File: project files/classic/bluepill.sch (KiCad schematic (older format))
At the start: 35 parts, among them J1 USB_B_Micro, J2 Boot, J3 Left Row, J4 Right Row, J5 SWD, SW1 Reset, U1 RT8183-33, U2 STM32F103C8Tx, Y1 8MHz, Y2 32768Hz

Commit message: re-arrangement + updated description
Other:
- note added: "BluePill boards from TaoBao have diferent design:\n+ extra 1M or 10M resistor between OSCIN | OSCOUT \n- no GND connection for capacitors\nSame concept can be found on some RedPill boards.\nRecommended design from STM has no resistor!\nIn this schematic it is OPTIONAL!\nBluePill uses crystal in HC-49S (HC-49-4H) package.\nBlackPill uses both: resistor (10M) and \ngrounding for capacitors.\nMapleM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"
- note added: "Typically used diodes:\n- 1N5819: in SOD123F or DO-41\n- LSM115JE3/TR13 : DO-214BA\n- BAS70 : in SOT23\n- 1N4448 : in SOD123\n- BAT54C : in SOT-23 : WeAct F4x1 DevBoards"
- note removed: "BluePill boards from TaoBao have diferent design:\n+ extra 1M or 10M resistor between OSCIN | OSCOUT \n- no GND connection for capacitors\nSame concept can be found on some RedPill boards.\nRecommended design from STM has no resistor!\nIn this schematic it is OPTIONAL!\nBluePill uses crystal in HC-49S (HC-49-4H) package.\nBlackPill uses both: resistor (10M) and \ngrounding for capacitors."
- note removed: "Typically used diodes:\n- 1N5819: in SOD123F or DO-41\n- LSM115JE3/TR13 : DO-214BA\n- BAS70 : in SOT23\n- 1N4448 : in SOD123"
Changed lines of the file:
@@
 	3000 1400 3500 1400
 Text Notes 550  3400 0    50   ~ 0
-It is recommended to install\nthe protection diode between Vbus and +5V!\n\nProtection diode is not installed on original BluePill, \nbut is sugested in order to protect computers USB\nport if  board is simulatneously pluged to computer\nand external power source.\nUsually it is either:\n- SS14 : in SMA (DO-214AC) Package\n- BAT54 : in SOT23\n- BAT60JFILM : up to 3A in SOD-323 case (Nucleo)\n- MBR0520LT1G : up to 0.5 A in SOD-123 Package\n- K24 : up to 2 A in SOD-123FL package (Black Pill)\n- PMEG2010EA : SOD323\n- STPS1L30A : SMA or SMA
+It is recommended to install\nthe protection diode between Vbus and +5V!\n\nProtection diode is not installed on original BluePill, \nbut is sugested in order to protect computers USB\nport if  board is simulatneously pluged to computer\nand external power source.\nUsually it is either:\n- SS14 : in SMA (DO-214AC) Package\n- BAT54 : in SOT23\n- BAT60JFILM : up to 3A in SOD-323 case (Nucleo)\n- MBR0520LT1G : up to 0.5 A in SOD-123 Package\n- K24 : up to 2 A in SOD-123FL package (Black Pill)\n- PMEG2010EA : SOD323\n- STPS1L30A : SMA or SMA\n- SD103*WS : SOD323 [marked S4] : MapleMini
 $Comp
 L power:+3.3V #PWR030
@@
 Text GLabel 7350 2850 2    50   Input ~ 0
 NRST
-Text Notes 4450 4100 0    50   ~ 0
-BluePill boards from TaoBao have diferent design:\n+ extra 1M or 10M resistor between OSCIN | OSCOUT \n- no GND connection for capacitors\nSame  concept can be found on some RedPill boards.\nRecommended design from STM has no resistor!\nIn this schematic it is OPTIONAL!\nBluePill uses crystal in HC-49S (HC-49-4H) package.\nBlackPill uses both: resistor (10M) and \ngrounding for capacitors.
+Text Notes 4450 4200 0    50   ~ 0
+BluePill boards from TaoBao have diferent design:\n+ extra 1M or 10M resistor between OSCIN | OSCOUT \n- no GND connection for capacitors\nSame  concept can be found on some RedPill boards.\nRecommended design from STM has no resistor!\nIn this schematic it is OPTIONAL!\nBluePill uses crystal in HC-49S (HC-49-4H) package.\nBlackPill uses both: resistor (10M) and \ngrounding for capacitors.\nMapleMinu uses AMB3AIG-8.000MHZ [5.0mm x 3.2 mm]
 $Comp
 L power:GNDREF #PWR028
@@
 PC13 : Green\nPower : Red
 Text Notes 9100 5800 0    50   ~ 0
-Typically used diodes:\n- 1N5819: in SOD123F or DO-41\n- LSM115JE3/TR13 : DO-214BA\n- BAS70 : in SOT23\n- 1N4448 : in SOD123
+Typically used diodes:\n- 1N5819: in SOD123F or DO-41\n- LSM115JE3/TR13 : DO-214BA\n- BAS70 : in SOT23\n- 1N4448 : in SOD123\n- BAT54C : in SOT-23 : WeAct F4x1 DevBoards
 Text Notes 700  6500 0    50   ~ 0
 Some clones uses AMS1117 as Linear Voltage Regulator\nwith tantalum SMD capacitors:\n- Pre-capacitor\n- Post-capacitor

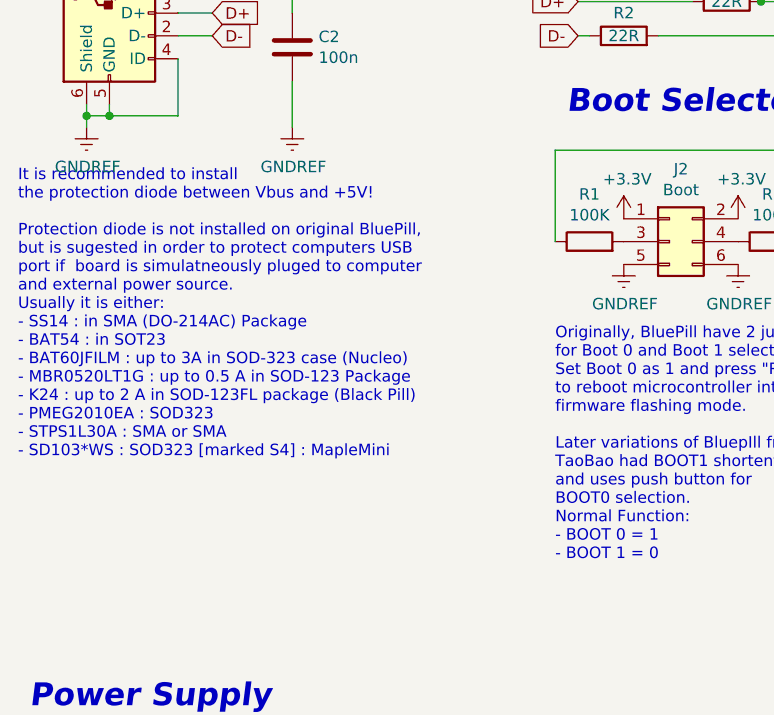
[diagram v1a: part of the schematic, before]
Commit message: replaced SWD 10 with 14
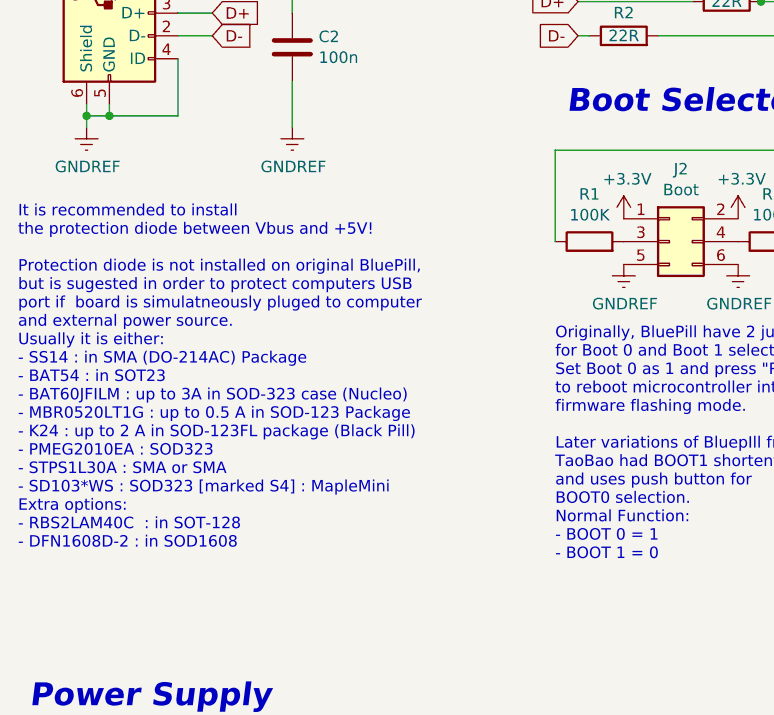
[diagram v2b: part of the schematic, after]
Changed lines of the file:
@@
 Wire Wire Line
 	3000 1400 3500 1400
-Text Notes 550  3400 0    50   ~ 0
-It is recommended to install\nthe protection diode between Vbus and +5V!\n\nProtection diode is not installed on original BluePill, \nbut is sugested in order to protect computers USB\nport if  board is simulatneously pluged to computer\nand external power source.\nUsually it is either:\n- SS14 : in SMA (DO-214AC) Package\n- BAT54 : in SOT23\n- BAT60JFILM : up to 3A in SOD-323 case (Nucleo)\n- MBR0520LT1G : up to 0.5 A in SOD-123 Package\n- K24 : up to 2 A in SOD-123FL package (Black Pill)\n- PMEG2010EA : SOD323\n- STPS1L30A : SMA or SMA\n- SD103*WS : SOD323 [marked S4] : MapleMini
+Text Notes 550  3800 0    50   ~ 0
+It is recommended to install\nthe protection diode between Vbus and +5V!\n\nProtection diode is not installed on original BluePill, \nbut is sugested in order to protect computers USB\nport if  board is simulatneously pluged to computer\nand external power source.\nUsually it is either:\n- SS14 : in SMA (DO-214AC) Package\n- BAT54 : in SOT23\n- BAT60JFILM : up to 3A in SOD-323 case (Nucleo)\n- MBR0520LT1G : up to 0.5 A in SOD-123 Package\n- K24 : up to 2 A in SOD-123FL package (Black Pill)\n- PMEG2010EA : SOD323\n- STPS1L30A : SMA or SMA\n- SD103*WS : SOD323 [marked S4] : MapleMini\nExtra options:\n- RBS2LAM40C  : in SOT-128\n- DFN1608D-2 : in SOD1608
 $Comp
 L power:+3.3V #PWR030

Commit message: re-routing
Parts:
- added C15: 100n, Capacitor_SMD:C_0603_1608Metric_Pad1.05x0.95mm_HandSolder, symbol Device:C
- added D3: SD103AWS, Diode_SMD:D_SOD-323, symbol Device:D_Schottky
- added D4: BAT54C, Package_TO_SOT_SMD:SOT-23, symbol Diode:BAT54C
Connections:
- net +3V3: now also D4.2
- net +5V: now also D3.1 (K); no longer C2.1, J1.1 (VBUS)
- net +BATT: now also D4.1; no longer U2.1 (VBAT)
- net GNDREF: now also C15.2
- net PC14: now also C8.1, Y2.4; no longer C6.1, Y2.1
- net PC15: now also C6.1, Y2.1; no longer C8.1, Y2.4
- new net VBUS: C2.1, D3.2 (A), J1.1 (VBUS)
- new net Vbat_protected: C15.1, D4.3, U2.1 (VBAT)
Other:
- note added: "Not Present on original BluePill.\nHighly recomended."
- note added: "Protection diode is not installed on original BluePill, \nbut is sugested in order to protect computers USB\nport if board is simulatneously pluged to computer\nand external power source.\nUsually it is either:\n- SS14 : in SMA (DO-214AC) Package\n- BAT54 : in SOT23\n- BAT60JFILM : up to 3A in SOD-323 case (Nucleo)\n- MBR0520LT1G : up to 0.5 A in SOD-123 Package\n- K24 : up to 2 A in SOD-123FL pa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"
- note removed: "It is recommended to install\nthe protection diode between Vbus and +5V!\n\nProtection diode is not installed on original BluePill, \nbut is sugested in order to protect computers USB\nport if board is simulatneously pluged to computer\nand external power source.\nUsually it is either:\n- SS14 : in SMA (DO-214AC) Package\n- BAT54 : in SOT23\n- BAT60JFILM : up to 3A in SOD-323 case (Nucleo)\n- MBR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"
- note removed: "Not Present on original BluePill.\nHighly recomended.\n\nPass the 3V3 and Vbat from header through\nseparate (individual) diodes.\nMerge behind diodes, decouple with 100nF.\nProvide this to Vbat of microcontroller."
- moved on the sheet: C10, J5
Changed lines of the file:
@@
 L Connector_Generic:Conn_01x04 J5
 U 1 1 5DE0F7EB
-P 8150 5250
-F 0 "J5" H 8230 5242 50  0000 L CNN
-F 1 "SWD" H 8230 5151 50  0000 L CNN
-F 2 "Connector_PinHeader_2.54mm:PinHeader_1x04_P2.54mm_Horizontal" H 8150 5250 50  0001 C CNN
-F 3 "~" H 8150 5250 50  0001 C CNN
-	1    8150 5250
+P 8450 5150
+F 0 "J5" H 8530 5142 50  0000 L CNN
+F 1 "SWD" H 8530 5051 50  0000 L CNN
+F 2 "Connector_PinHeader_2.54mm:PinHeader_1x04_P2.54mm_Horizontal" H 8450 5150 50  0001 C CNN
+F 3 "~" H 8450 5150 50  0001 C CNN
+	1    8450 5150
 	1    0    0    1
 $EndComp
@@
 L Device:C C10
 U 1 1 5E02788D
-P 7350 5200
-F 0 "C10" H 7235 5154 50  0000 R CNN
-F 1 "100n" H 7235 5245 50  0000 R CNN
-F 2 "Capacitor_SMD:C_0603_1608Metric_Pad1.05x0.95mm_HandSolder" H 7388 5050 50  0001 C CNN
-F 3 "~" H 7350 5200 50  0001 C CNN
-	1    7350 5200
+P 7650 5100
+F 0 "C10" H 7535 5054 50  0000 R CNN
+F 1 "100n" H 7535 5145 50  0000 R CNN
+F 2 "Capacitor_SMD:C_0603_1608Metric_Pad1.05x0.95mm_HandSolder" H 7688 4950 50  0001 C CNN
+F 3 "~" H 7650 5100 50  0001 C CNN
+	1    7650 5100
 	-1   0    0    1
 $EndComp
 Wire Wire Line
-	7950 5050 7350 5050
-Wire Wire Line
-	7350 5350 7950 5350
+	8250 4950 7650 4950
+Wire Wire Line
+	7650 5250 8250 5250
 $Comp
 L power:+3.3V #PWR09
@@
 	3000 1400 3500 1400
 Text Notes 550  3800 0    50   ~ 0
-It is recommended to install\nthe protection diode between Vbus and +5V!\n\nProtection diode is not installed on original BluePill, \nbut is sugested in order to protect computers USB\nport if  board is simulatneously pluged to computer\nand external power source.\nUsually it is either:\n- SS14 : in SMA (DO-214AC) Package\n- BAT54 : in SOT23\n- BAT60JFILM : up to 3A in SOD-323 case (Nucleo)\n- MBR0520LT1G : up to 0.5 A in SOD-123 Package\n- K24 : up to 2 A in SOD-123FL package (Black Pill)\n- PMEG2010EA : SOD323\n- STPS1L30A : SMA or SMA\n- SD103*WS : SOD323 [marked S4] : MapleMini\nExtra options:\n- RBS2LAM40C  : in SOT-128\n- DFN1608D-2 : in SOD1608
+Protection diode is not installed on original BluePill, \nbut is sugested in order to protect computers USB\nport if  board is simulatneously pluged to computer\nand external power source.\nUsually it is either:\n- SS14 : in SMA (DO-214AC) Package\n- BAT54 : in SOT23\n- BAT60JFILM : up to 3A in SOD-323 case (Nucleo)\n- MBR0520LT1G : up to 0.5 A in SOD-123 Package\n- K24 : up to 2 A in SOD-123FL package (Black Pill)\n- PMEG2010EA : SOD323\n- STPS1L30A : SMA or SMA\n- SD103*WS : SOD323 [marked S4] : MapleMini\nExtra options:\n- RBS2LAM40C  : in SOT-128\n- DFN1608D-2 : in SOD1608
 $Comp
 L power:+3.3V #PWR030
 U 1 1 5E0B07ED
-P 7350 5000
-F 0 "#PWR030" H 7350 4850 50  0001 C CNN
-F 1 "+3.3V" H 7365 5128 50  0000 L CNN
-F 2 "" H 7350 5000 50  0001 C CNN
-F 3 "" H 7350 5000 50  0001 C CNN
-	1    7350 5000
+P 7650 4900
+F 0 "#PWR030" H 7650 4750 50  0001 C CNN
+F 1 "+3.3V" H 7665 5028 50  0000 L CNN
+F 2 "" H 7650 4900 50  0001 C CNN
+F 3 "" H 7650 4900 50  0001 C CNN
+	1    7650 4900
 	1    0    0    -1
 $EndComp
@@
 L power:GNDREF #PWR031
 U 1 1 5E0B0BD6
-P 7350 5400
-F 0 "#PWR031" H 7350 5150 50  0001 C CNN
-F 1 "GNDREF" H 7355 5227 50  0000 C CNN
-F 2 "" H 7350 5400 50  0001 C CNN
-F 3 "" H 7350 5400 50  0001 C CNN
-	1    7350 5400
-	1    0    0    -1
-$EndComp
-Wire Wire Line
-	7350 5050 7350 5000
-Connection ~ 7350 5050
-Wire Wire Line
-	7350 5400 7350 5350
-Connection ~ 7350 5350
+P 7650 5300
+F 0 "#PWR031" H 7650 5050 50  0001 C CNN
+F 1 "GNDREF" H 7655 5127 50  0000 C CNN
+F 2 "" H 7650 5300 50  0001 C CNN
+F 3 "" H 7650 5300 50  0001 C CNN
+	1    7650 5300
+	1    0    0    -1
+$EndComp
+Wire Wire Line
+	7650 4950 7650 4900
+Connection ~ 7650 4950
+Wire Wire Line
+	7650 5300 7650 5250
+Connection ~ 7650 5250
 $Comp
 L Connector_Generic:Conn_01x20 J4
@@
 L power:+5V #PWR06
 U 1 1 5E127D96
-P 1950 1200
-F 0 "#PWR06" H 1950 1050 50  0001 C CNN
-F 1 "+5V" H 1965 1373 50  0000 C CNN
-F 2 "" H 1950 1200 50  0001 C CNN
-F 3 "" H 1950 1200 50  0001 C CNN
-	1    1950 1200
-	1    0    0    -1
-$EndComp
-Wire Wire Line
-	1950 1200 1950 1250
+P 2150 1200
+F 0 "#PWR06" H 2150 1050 50  0001 C CNN
+F 1 "+5V" H 2165 1373 50  0000 C CNN
+F 2 "" H 2150 1200 50  0001 C CNN
+F 3 "" H 2150 1200 50  0001 C CNN
+	1    2150 1200
+	1    0    0    -1
+$EndComp
 Wire Wire Line
 	3050 1550 3000 1550
@@
 Wire Wire Line
 	6800 950  6800 1150
+Text GLabel 5400 1000 2    50   Input ~ 0
+PC14
 Text GLabel 5400 800  2    50   Input ~ 0
-PC14
-Text GLabel 5400 1000 2    50   Input ~ 0
 PC15
 Text GLabel 8350 2050 0    50   Input ~ 0
@@
 Wire Wire Line
 	5200 6750 5200 6850
-Text GLabel 7950 5150 0    50   Input ~ 0
+Text GLabel 8250 5050 0    50   Input ~ 0
 SWDIO
-Text GLabel 7950 5250 0    50   Input ~ 0
+Text GLabel 8250 5150 0    50   Input ~ 0
 SWCLK
-Text GLabel 7500 5750 0    50   Input ~ 0
+Text GLabel 7800 5650 0    50   Input ~ 0
 SWO
-Text GLabel 8000 5750 2    50   Input ~ 0
+Text GLabel 8300 5650 2    50   Input ~ 0
 PB3
 Wire Wire Line
-	7500 5750 8000 5750
-Text Notes 7250 4750 0    100  Italic 20
+	7800 5650 8300 5650
+Text Notes 7550 4650 0    100  Italic 20
 SWD interface
 $Comp
@@
 L power:VBUS #PWR04
 U 1 1 5DED193B
-P 1750 1200
-F 0 "#PWR04" H 1750 1050 50  0001 C CNN
-F 1 "VBUS" H 1765 1373 50  0000 C CNN
-F 2 "" H 1750 1200 50  0001 C CNN
-F 3 "" H 1750 1200 50  0001 C CNN
-	1    1750 1200
+P 1350 1200
+F 0 "#PWR04" H 1350 1050 50  0001 C CNN
+F 1 "VBUS" H 1365 1373 50  0000 C CNN
+F 2 "" H 1350 1200 50  0001 C CNN
+F 3 "" H 1350 1200 50  0001 C CNN
+	1    1350 1200
 	1    0    0    -1
 $EndComp
@@
 $EndComp
 Wire Wire Line
-	1250 1250 1750 1250
+	1250 1250 1350 1250
 Wire Wire Line
 	1750 1450 1750 1250
-Connection ~ 1750 1250
-Wire Wire Line
-	1750 1250 1950 1250
-Wire Wire Line
-	1750 1200 1750 1250
 $Comp
 L power:GNDREF #PWR05
@@
 Text Notes 6800 1800 0    50   ~ 0
 PC13 : Green\nPower : Red
-Text Notes 9100 5800 0    50   ~ 0
+Text Notes 9100 6450 0    50   ~ 0
 Typically used diodes:\n- 1N5819: in SOD123F or DO-41\n- LSM115JE3/TR13 : DO-214BA\n- BAS70 : in SOT23\n- 1N4448 : in SOD123\n- BAT54C : in SOT-23 : WeAct F4x1 DevBoards
 Text Notes 700  6500 0    50   ~ 0
 Some clones uses AMS1117 as Linear Voltage Regulator\nwith tantalum SMD capacitors:\n- Pre-capacitor\n- Post-capacitor
+Text Notes 9100 5950 0    50   ~ 0
+Not Present on original BluePill.\nHighly recomended.
+$Comp
+L Device:D_Schottky D3
+U 1 1 5E178BE9
+P 1900 1250
+F 0 "D3" H 1900 1034 50  0000 C CNN
+F 1 "SD103AWS" H 1900 1125 50  0000 C CNN
+F 2 "Diode_SMD:D_SOD-323" H 1900 1250 50  0001 C CNN
+F 3 "~" H 1900 1250 50  0001 C CNN
+	1    1900 1250
+	-1   0    0    1
+$EndComp
+Connection ~ 1750 1250
+Wire Wire Line
+	2050 1250 2150 1250
+Wire Wire Line
+	2150 1250 2150 1200
+Wire Wire Line
+	1350 1200 1350 1250
+Connection ~ 1350 1250
+Wire Wire Line
+	1350 1250 1750 1250
+Text GLabel 8900 900  2    50   Input ~ 0
+Vbat_protected
+Wire Wire Line
+	8900 900  8850 900
+Text GLabel 9550 5250 2    50   Input ~ 0
+Vbat_protected
+$Comp
+L Diode:BAT54C D4
+U 1 1 5E189BAD
+P 9450 5050
+F 0 "D4" H 9450 5275 50  0000 C CNN
+F 1 "BAT54C" H 9450 5184 50  0000 C CNN
+F 2 "Package_TO_SOT_SMD:SOT-23" H 9525 5175 50  0001 L CNN
+F 3 "http://www.diodes.com/_files/datasheets/ds11005.pdf" H 9370 5050 50  0001 C CNN
+	1    9450 5050
+	1    0    0    -1
+$EndComp
+$Comp
+L Device:C C15
+U 1 1 5E18C388
+P 9450 5400
+F 0 "C15" H 9565 5446 50  0000 L CNN
+F 1 "100n" H 9565 5355 50  0000 L CNN
+F 2 "Capacitor_SMD:C_0603_1608Metric_Pad1.05x0.95mm_HandSolder" H 9488 5250 50  0001 C CNN
+F 3 "~" H 9450 5400 50  0001 C CNN
+	1    9450 5400
+	1    0    0    -1
+$EndComp
+Wire Wire Line
+	9550 5250 9450 5250
+Connection ~ 9450 5250
+$Comp
+L power:GNDREF #PWR040
+U 1 1 5E195578
+P 9450 5550
+F 0 "#PWR040" H 9450 5300 50  0001 C CNN
+F 1 "GNDREF" H 9455 5377 50  0000 C CNN
+F 2 "" H 9450 5550 50  0001 C CNN
+F 3 "" H 9450 5550 50  0001 C CNN
+	1    9450 5550
+	1    0    0    -1
+$EndComp
 $Comp
 L power:+BATT #PWR033
-U 1 1 5E161622
-P 8850 900
-F 0 "#PWR033" H 8850 750 50  0001 C CNN
-F 1 "+BATT" H 8865 1027 50  0000 L CNN
-F 2 "" H 8850 900 50  0001 C CNN
-F 3 "" H 8850 900 50  0001 C CNN
-	1    8850 900
-	1    0    0    -1
-$EndComp
-Text Notes 9100 5350 0    50   ~ 0
-Not Present on original BluePill.\nHighly recomended.\n\nPass the 3V3 and Vbat from header through\nseparate (individual) diodes.\nMerge behind diodes, decouple with 100nF.\nProvide this to Vbat of microcontroller.
+U 1 1 5E19686F
+P 9150 4950
+F 0 "#PWR033" H 9150 4800 50  0001 C CNN
+F 1 "+BATT" H 9165 5123 50  0000 C CNN
+F 2 "" H 9150 4950 50  0001 C CNN
+F 3 "" H 9150 4950 50  0001 C CNN
+	1    9150 4950
+	1    0    0    -1
+$EndComp
+$Comp
+L power:+3.3V #PWR041
+U 1 1 5E1982AA
+P 9750 4950
+F 0 "#PWR041" H 9750 4800 50  0001 C CNN
+F 1 "+3.3V" H 9765 5123 50  0000 C CNN
+F 2 "" H 9750 4950 50  0001 C CNN
+F 3 "" H 9750 4950 50  0001 C CNN
+	1    9750 4950
+	1    0    0    -1
+$EndComp
+Wire Wire Line
+	9750 5050 9750 4950
+Wire Wire Line
+	9150 5050 9150 4950
 $EndSCHEMATC
